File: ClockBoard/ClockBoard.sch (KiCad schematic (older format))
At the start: 14 parts

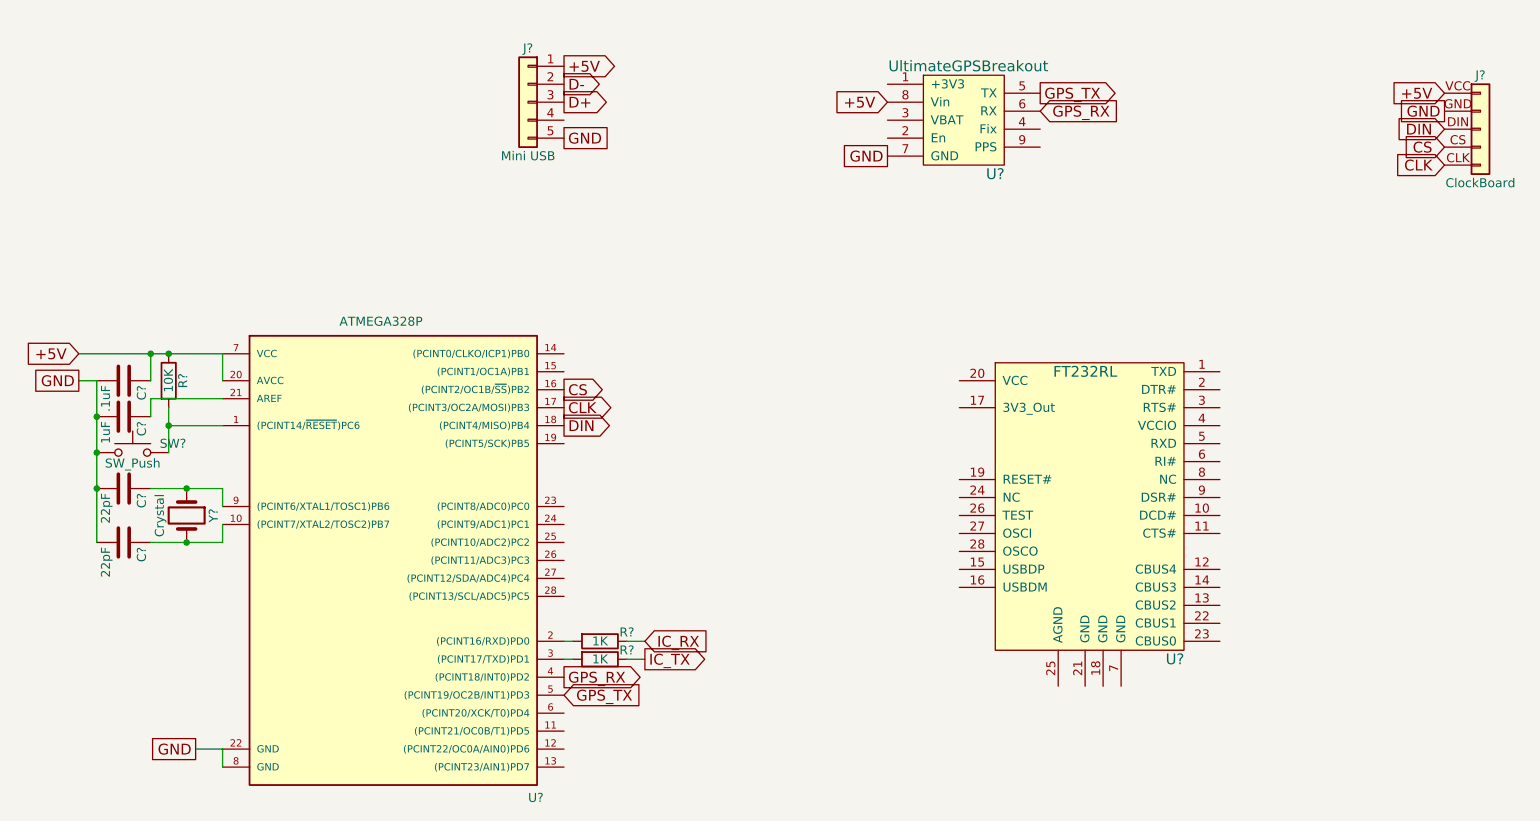
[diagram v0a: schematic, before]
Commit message: Created clock board
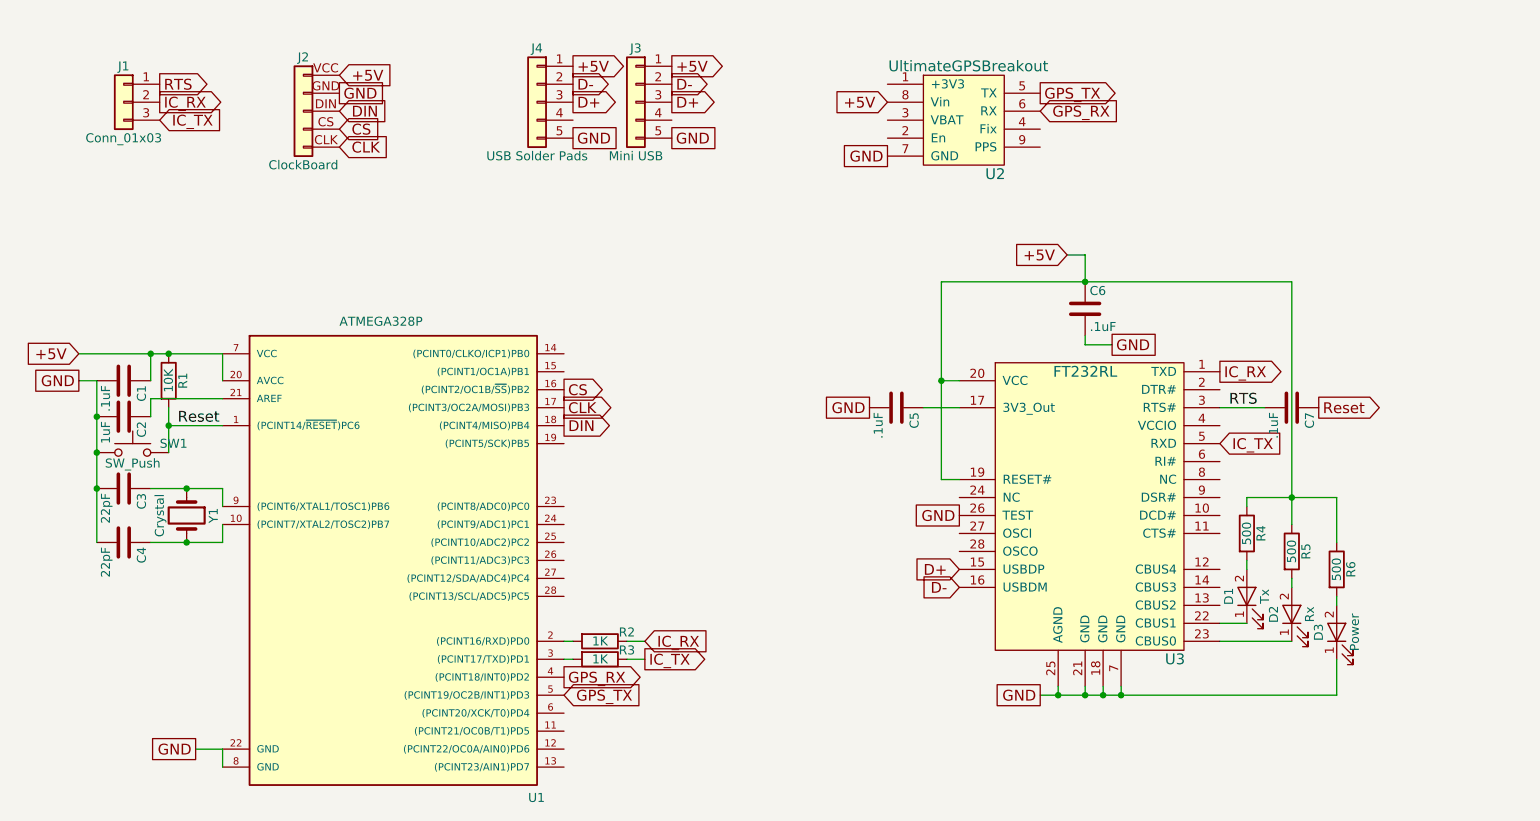
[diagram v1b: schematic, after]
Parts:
- added C5, C6, C7: .1uF, Capacitors_SMD:C_0603_HandSoldering, symbol C
- added D1: Tx, Diodes_SMD:D_0603, symbol LED
- added D2: Rx, Diodes_SMD:D_0603, symbol LED
- added D3: Power, Diodes_SMD:D_0603, symbol LED
- added J1: Conn_01x03, Pin_Headers:Pin_Header_Straight_1x03_Pitch2.54mm, symbol Conn_01x03
- added J4: USB Solder Pads, Pin_Headers:Pin_Header_Straight_1x05_Pitch2.54mm, symbol Conn_01x05
- added R4, R5, R6: 500, Resistors_SMD:R_0603_HandSoldering, symbol R
- C1, C2, C3, C4: renamed from C?; footprint (none) -> Capacitors_SMD:C_0603_HandSoldering
- J2: renamed from J?; footprint (none) -> Pin_Headers:Pin_Header_Straight_1x05_Pitch2.54mm
- J3: renamed from J?; footprint (none) -> Project_Library:MiniUSB_SMT
- R1, R2, R3: renamed from R?; footprint (none) -> Resistors_SMD:R_0603_HandSoldering
- SW1: renamed from SW?; footprint (none) -> Project_Library:SPST_Pushbutton
- U1: renamed from U?; footprint DIL28 -> Housings_DIP:DIP-28_W7.62mm
- U2: renamed from U?; footprint (none) -> Project_Library:Ultimate_GPS_Breakout
- U3: renamed from U?; footprint (none) -> Housings_SSOP:SSOP-28_5.3x10.2mm_Pitch0.65mm
- Y1: renamed from Y?; footprint (none) -> Crystals:Crystal_SMD_HC49-SD_HandSoldering
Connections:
- net +5V: now also U3.19 (RESET#), U3.20 (VCC), C6.1, J4.1 (Pin_1), R4.1, R5.1, R6.1
- net D+: now also U3.15 (USBDP), J4.3 (Pin_3)
- net D-: now also U3.16 (USBDM), J4.2 (Pin_2)
- net GND: now also U3.18 (GND), U3.21 (GND), U3.25 (AGND), U3.26 (TEST), U3.7 (GND), C5.2, C6.2, D3.1 (K), J4.5 (Pin_5)
- net IC_RX: now also U3.1 (TXD), J1.2 (Pin_2)
- net IC_TX: now also U3.5 (RXD), J1.3 (Pin_3)
- net at U3.17 (3V3_Out): now also C5.1
- net at U3.22 (CBUS1): now also D1.1 (K)
- net at U3.23 (CBUS0): now also D2.1 (K)
- net RTS: now reaches U3.3 (RTS#)
- net RTS: now also C7.2, J1.1 (Pin_1)
- net Reset: now reaches R1.2, SW1.2, U1.1 ((PCINT14/~RESET~)PC6)
- net Reset: now also C7.1
- new net: D1.2 (A), R4.2
- new net: D2.2 (A), R5.2
- new net: D3.2 (A), R6.2
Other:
- moved on the sheet: J2, J3

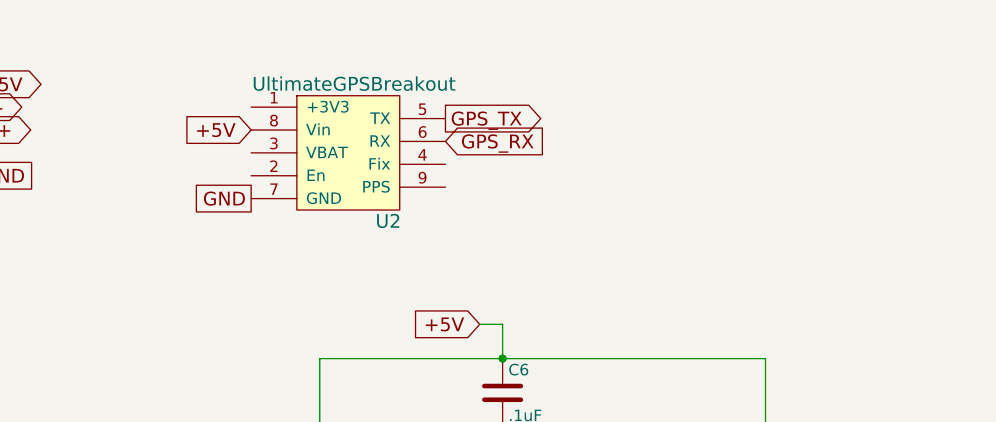
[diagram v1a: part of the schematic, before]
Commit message: Made Clock Board
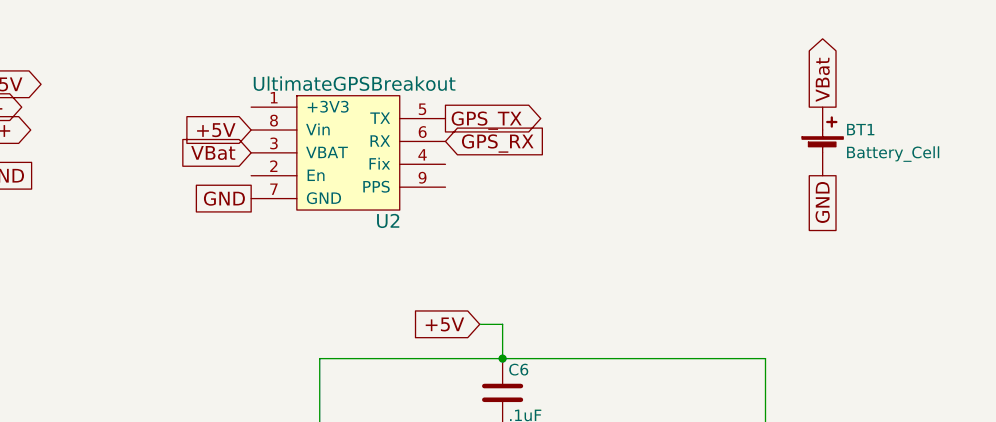
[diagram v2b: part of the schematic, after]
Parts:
- added BT1: Battery_Cell, Project_Library:CR1220_Battery_Holder, symbol Battery_Cell
- J2: footprint Pin_Headers:Pin_Header_Straight_1x05_Pitch2.54mm -> Project_Library:Clock_Board
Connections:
- net GND: now also BT1.2 (-)
- net VBat: now reaches U2.3 (VBAT)
- net VBat: now also BT1.1 (+)
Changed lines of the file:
@@
 F 0 "J2" H 2150 2150 50  0000 C CNN
 F 1 "ClockBoard" H 2150 1550 50  0000 C CNN
-F 2 "Pin_Headers:Pin_Header_Straight_1x05_Pitch2.54mm" H 2150 1850 50  0001 C CNN
+F 2 "Project_Library:Clock_Board" H 2150 1850 50  0001 C CNN
 F 3 "" H 2150 1850 50  0001 C CNN
 	1    2150 1850
@@
 Text GLabel 3650 2000 2    60   UnSpc ~ 0
 GND
+$Comp
+L Battery_Cell BT1
+U 1 1 5B74380B
+P 7900 1900
+F 0 "BT1" H 8000 2000 50  0000 L CNN
+F 1 "Battery_Cell" H 8000 1900 50  0000 L CNN
+F 2 "Project_Library:CR1220_Battery_Holder" V 7900 1960 50  0001 C CNN
+F 3 "" V 7900 1960 50  0001 C CNN
+	1    7900 1900
+	1    0    0    -1
+$EndComp
+Text GLabel 5400 1900 0    60   Input ~ 0
+VBat
+Text GLabel 7900 1700 1    60   Output ~ 0
+VBat
+Text GLabel 7900 2000 3    60   UnSpc ~ 0
+GND
 $EndSCHEMATC
